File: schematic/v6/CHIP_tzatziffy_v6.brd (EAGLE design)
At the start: 40.9 x 49.8 mm, 51 parts, among them J1 2X20-CHIP0.8_DRILL, J3 S2B-PH-SM4-TB, Q1 NPN-DTC114YUA, Q2 PNP-DTA114YUA, U1 LMR62421, U3 DS2431P, X1 FH12-40S-0.5SH

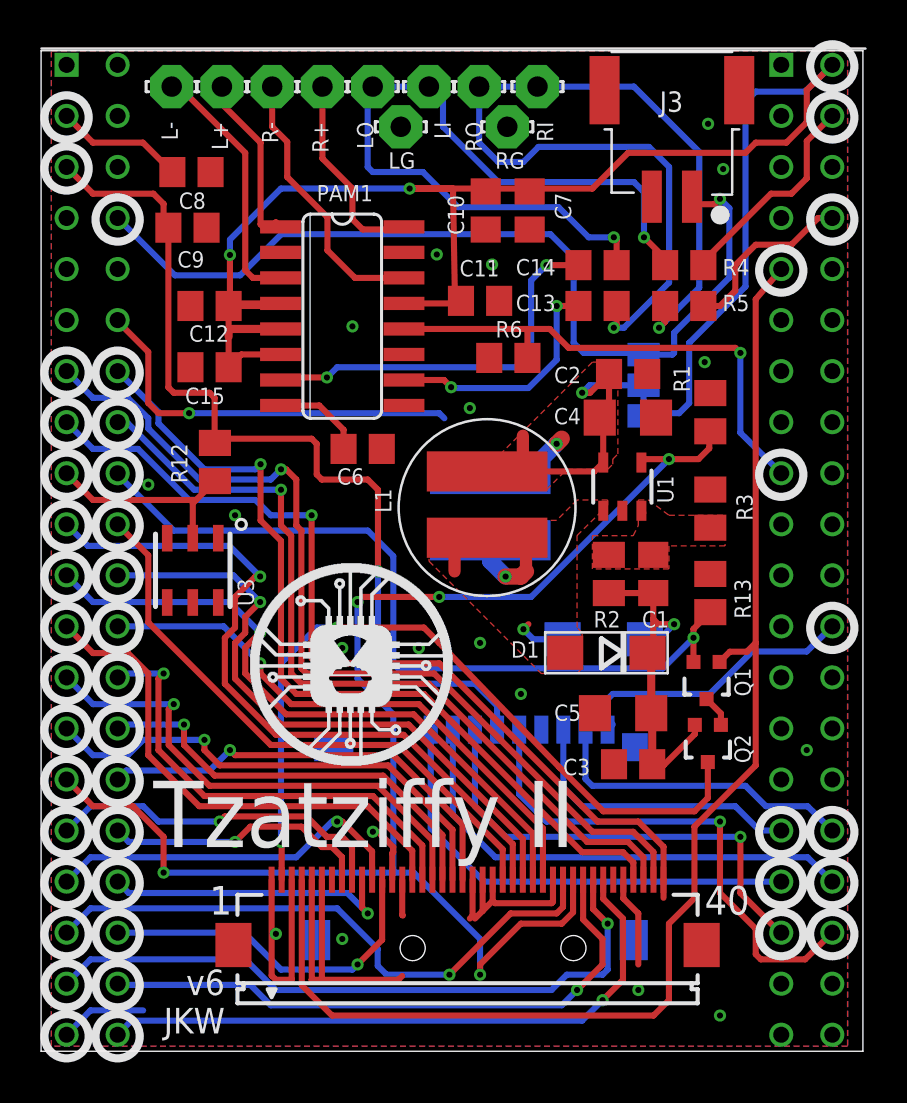
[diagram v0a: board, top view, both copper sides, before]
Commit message: Added pads for power button and vias for the uart header
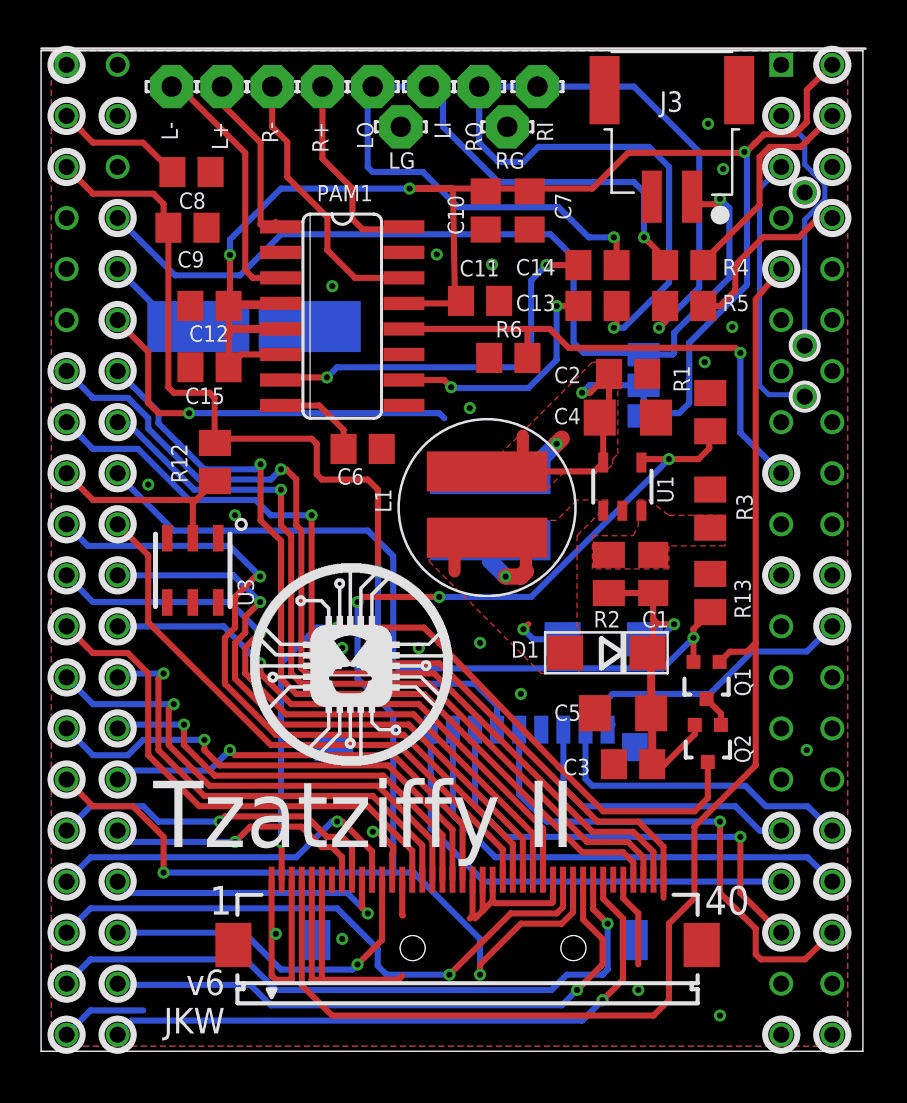
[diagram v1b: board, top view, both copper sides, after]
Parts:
- added BTN: BTN, wirepad:SMD2,54-5,08
- added GND: GND, wirepad:SMD2,54-5,08
- moved U$4 0.76 mm to (6.67, 37.8)
- moved U$3 0.50 mm to (17.5, 37.3)
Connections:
- net GND: now also GND.1
- net PWR_ON: now also BTN.1
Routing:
- net UART_RX: track 0.00 -> 13.8 mm, vias 0 -> 1
- net UART_TX: track 0.00 -> 12.7 mm, vias 0 -> 1
- net VCC5V: track 109.8 -> 102.4 mm, vias 4 -> 5
- net PWR_ON: track 0.00 -> 5.20 mm
- net GND: vias 20 -> 22

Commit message: changed poti pins to smaller restring, added jumper for 3.3/5/vbat for DC/DC and 3.3/5 for audio amp
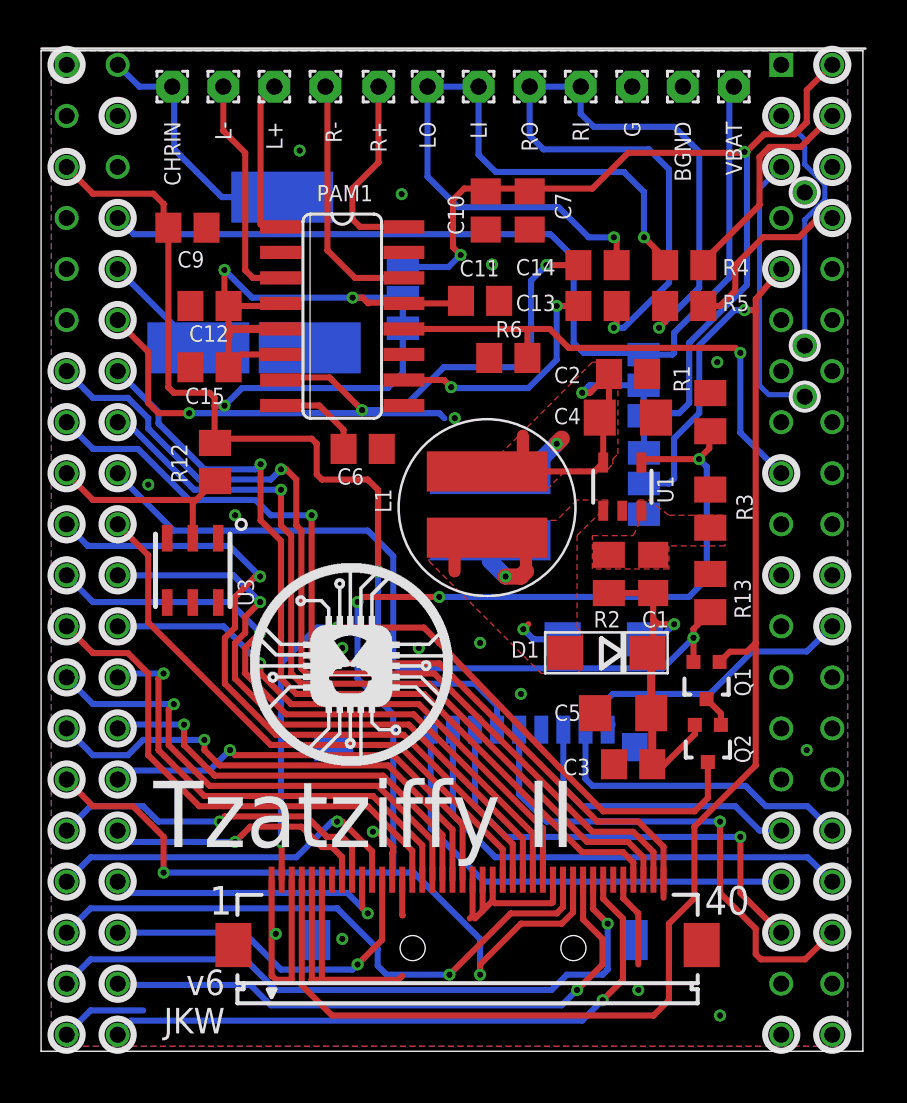
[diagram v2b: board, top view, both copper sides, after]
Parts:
- removed C8: n.a., rcl:C0805
- removed J3: S2B-PH-SM4-TB, Keyboard v0_5:S2B-PH-SM4-TB
- removed LG, RG: LSP10, solpad:LSP10
- added BGND, CHRIN, G, VBAT: (no value), wirepad:1,6/0,8
- added CHRIN_P: CHRIN, wirepad:SMD2,54-5,08
- added SJ2, SJ3: (no value), SparkFun-Retired:SJ_2
- L+, L-, LI, LO, R+, R-, RI, RO: value LSP10 -> (none); device solpad:LSP10 -> wirepad:1,6/0,8
- moved U$3 38.0 mm to (6.21, 1.08)
- moved U$4 29.1 mm to (5.79, 8.65)
- moved R+ 2.79 mm to (16.8, 48.0), turned to 0 degrees
- moved LO 2.73 mm to (19.2, 48.0)
- moved R- 2.65 mm to (14.2, 48.0)
- moved L+ 2.61 mm to (11.6, 48.0), turned to 0 degrees
- moved L- 2.57 mm to (9.07, 48.0), turned to 0 degrees
- moved RO 2.51 mm to (24.3, 48.0)
- moved LI 2.47 mm to (21.8, 48.0)
- moved RI 2.15 mm to (26.9, 48.0)
- moved U$5 1.55 mm to (5.97, 20.9)
- moved BTN 1.06 mm to (7.83, 35.0)
- moved GND 1.06 mm to (13.4, 35.0)
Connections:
- removed net N$9: C8.1, J1.VCC5V@0
- new net N$24: CHRIN.1, CHRIN_P.1, J1.CHG-IN
- new net VCC-5V: J1.VCC5V@0
- net GND: now also BGND.1, G.1; no longer C8.2, J3.2, LG.MP, RG.MP
- net N$26: now also SJ2.2
- net N$32: now also L+.1; no longer L+.MP
- net N$33: now also L-.1; no longer L-.MP
- net N$34: now also R+.1; no longer R+.MP
- net N$35: now also R-.1; no longer R-.MP
- net N$41: now also LI.1, LO.1; no longer LI.MP, LO.MP
- net N$43: now also RI.1, RO.1; no longer RI.MP, RO.MP
- net VBAT_EXT: now also VBAT.1; no longer J3.1
- net VCC3V3: now also C11.2, C12.2, C15.1, PAM1.13, PAM1.4, PAM1.5, PAM1.6, SJ3.2, SJ3.3
- net VCC5V: now also SJ2.3, SJ3.1; no longer C11.2, C12.2, C15.1, PAM1.13, PAM1.4, PAM1.5, PAM1.6
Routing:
- net VCC3V3: track 47.0 -> 89.4 mm, vias 1 -> 4
- net VCC5V: track 102.4 -> 70.2 mm, vias 5 -> 4
- net N$24: track 0.00 -> 12.7 mm
- net N$26: track 65.3 -> 77.6 mm, vias 0 -> 1
- net N$9: track 6.43 -> 0.00 mm
- net EN: track 71.8 -> 77.3 mm
- net N$43: track 47.0 -> 41.9 mm
- net N$41: track 39.8 -> 35.4 mm
- net PWR_ON: track 5.20 -> 7.21 mm
- net VBAT_EXT: track 45.8 -> 47.5 mm, vias 1 -> 0
- net N$36: track 19.3 -> 20.6 mm
- net N$33: track 12.8 -> 11.5 mm
- net N$35: track 13.7 -> 12.6 mm
- net N$32: track 8.99 -> 8.29 mm
- net N$34: track 10.5 -> 9.86 mm
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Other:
- board text added: "A"
- board text added: "A:3v3 B:5v C:Bat"
- board text added: "Amp"
- board text added: "B"
- board text added: "BGND"
- board text added: "C"
- board text added: "CHRIN"
- board text added: "DC/DC"
- board text added: "G"
- board text added: "VBAT"
- board text removed: "A B"
- board text removed: "A:5v (def) B:Battery"
- board text removed: "LG"
- board text removed: "RG"

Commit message: replaced bipolar with mosfet circuit and relayouted
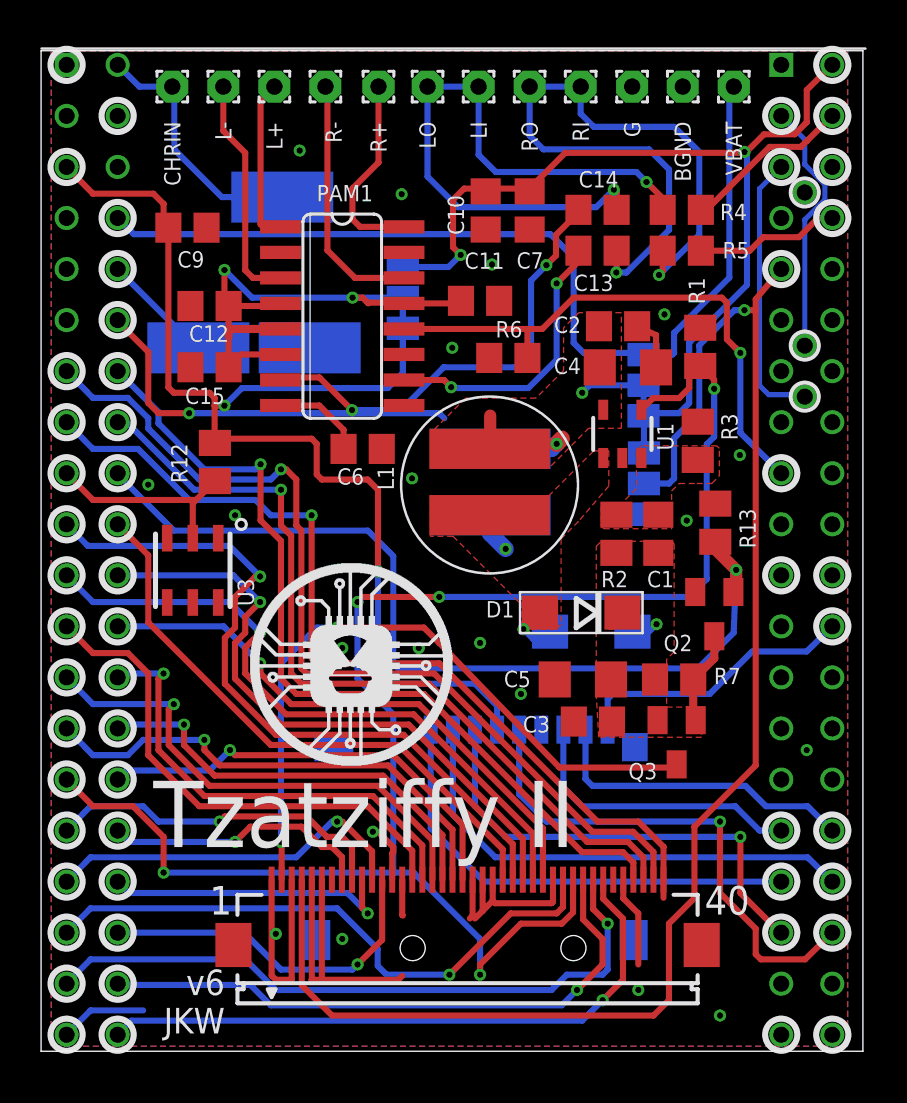
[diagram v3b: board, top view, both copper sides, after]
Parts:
- removed Q1: NPN-DTC114YUA, PocketCHIP-Components-v0.72:SOT323
- added Q3: BSS7728NH6327XTSA2, transistor-small-signal:SOT23
- added R7: 10k, rcl:M0805
- Q2: value PNP-DTA114YUA -> 2N7002ET1G; device PocketCHIP-Components-v0.72:SOT323 -> transistor-small-signal:SOT23
- R13: value 1.2K -> 10K
- moved Q2 6.44 mm to (33.5, 21.8)
- moved R13 3.51 mm to (33.5, 26.3)
- moved R3 3.43 mm to (32.7, 30.4)
- moved R1 3.29 mm to (32.8, 35.0)
- moved C3 2.92 mm to (27.5, 16.4)
- moved R4 2.75 mm to (31.9, 41.9)
- moved R5 2.75 mm to (31.9, 39.8)
- moved C13 2.75 mm to (27.7, 39.8)
- moved C14 2.75 mm to (27.7, 41.9)
- moved U1 2.62 mm to (28.9, 30.7)
- moved C5 2.61 mm to (27.0, 18.5)
- moved C4 2.50 mm to (29.2, 34.0)
- moved C2 2.43 mm to (28.7, 36.1)
- moved D1 2.36 mm to (26.9, 21.8)
- moved R2 2.03 mm to (28.6, 25.7)
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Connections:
- removed net N$63: Q1.3, Q2.1
- new net N$9: Q2.3, Q3.1, R7.2
- net GND: now also Q2.2
- net N$26: no longer Q1.1
- net N$61: now also Q3.3; no longer Q2.3
- net PWM: now also Q2.1; no longer Q1.2
- net PWR_LGT: now also Q3.2, R7.1; no longer Q2.2
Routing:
- net PWR_LGT: track 18.5 -> 3.99 mm
- net VCC5V: track 70.2 -> 57.1 mm
- net VREG_OUTPUT: track 12.5 -> 4.78 mm
- net N$43: track 41.9 -> 36.5 mm
- net PWM: track 39.3 -> 44.7 mm
- net N$9: track 0.00 -> 4.66 mm
- net EN: track 77.3 -> 81.8 mm
- net N$61: track 38.7 -> 34.2 mm
- net N$41: track 35.4 -> 32.4 mm
- net N$40: track 11.5 -> 8.47 mm
- net GP3: track 25.5 -> 28.2 mm
- net GND: track 68.7 -> 71.3 mm, vias 19 -> 22
- net N$26: track 77.6 -> 75.4 mm
- net N$39: track 12.1 -> 14.2 mm
- net N$36: track 20.6 -> 22.4 mm
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- added copper zone on layer 1, net PWR_LGT

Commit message: simplyfied the backlight driver ... a lot
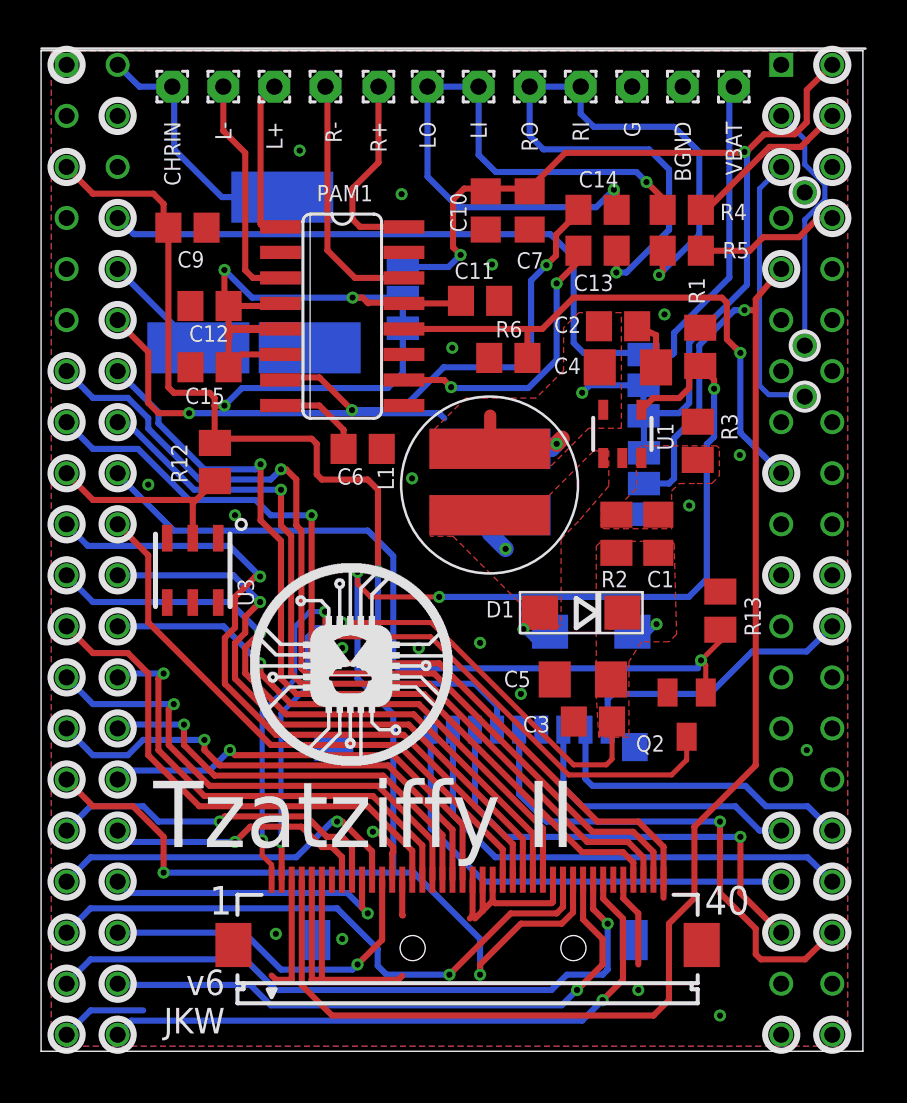
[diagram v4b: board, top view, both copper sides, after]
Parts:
- removed Q3: BSS7728NH6327XTSA2, transistor-small-signal:SOT23
- removed R7: 10k, rcl:M0805
- moved Q2 5.19 mm to (32.1, 16.8)
- moved R13 4.38 mm to (33.8, 21.9)
- moved U$4 1.43 mm to (6.17, 10.0)
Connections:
- removed net N$61: Q3.3, X1.2
- removed net N$9: Q2.3, Q3.1, R7.2
- new net DISPL_GND: Q2.3, X1.1
- net GND: no longer X1.1
- net PWR_LGT: now also X1.2; no longer Q3.2, R7.1
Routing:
- net DISPL_GND: track 0.00 -> 38.7 mm, vias 0 -> 2
- net N$61: track 34.2 -> 0.00 mm, vias 2 -> 0
- net PWR_LGT: track 3.99 -> 36.9 mm, vias 1 -> 3
- net GND: track 71.3 -> 66.6 mm
- net N$9: track 4.66 -> 0.00 mm
- net PWM: track 44.7 -> 40.2 mm
- net EN: track 81.8 -> 84.0 mm

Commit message: changed holes size to 0.7mm
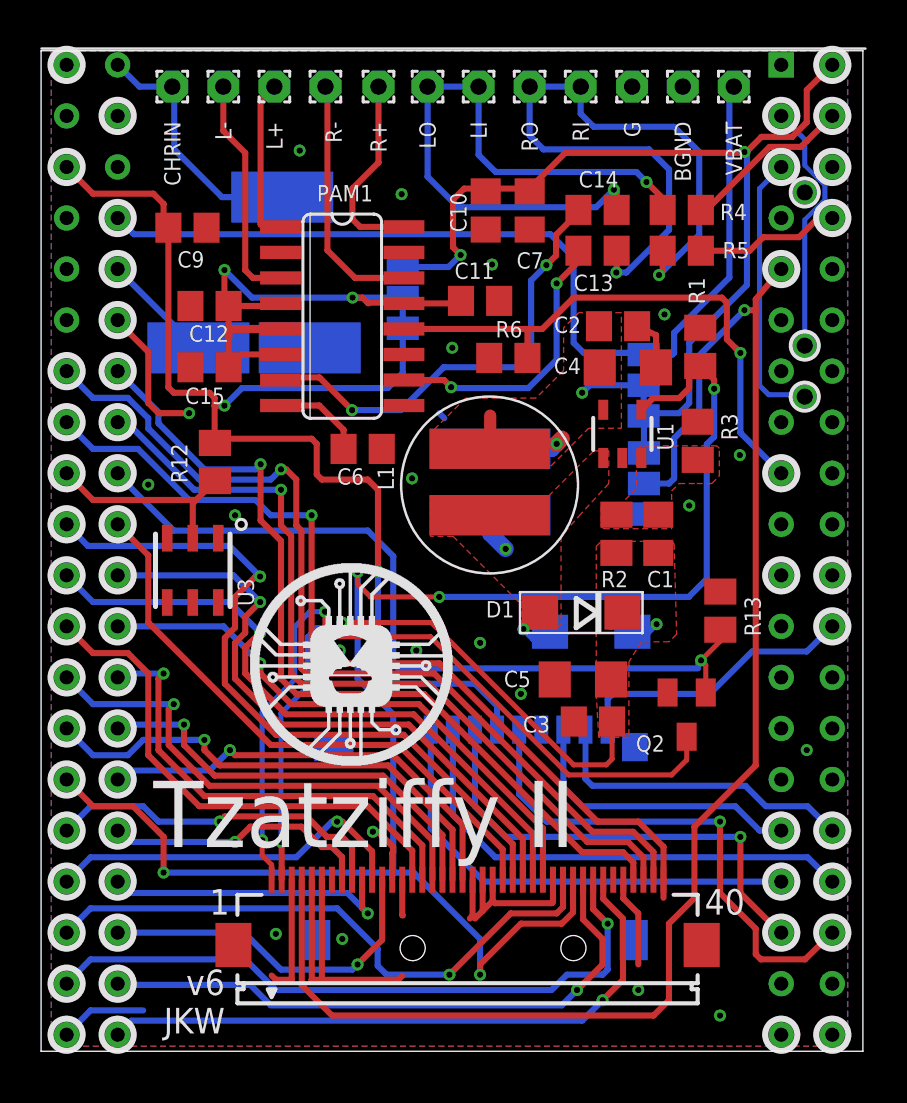
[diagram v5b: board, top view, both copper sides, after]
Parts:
- J1: value 2X20-CHIP0.8_DRILL -> 2X20-CHIP0.7_DRILL; device JKW_CHIP:2X20CHIP_NOOFFSET-TH_0.8 -> JKW_CHIP:2X20CHIP_NOOFFSET-TH_0.7
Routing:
- net GND: track 66.6 -> 54.1 mm
